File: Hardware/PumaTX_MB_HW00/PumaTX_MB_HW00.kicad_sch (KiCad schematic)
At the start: 5 parts

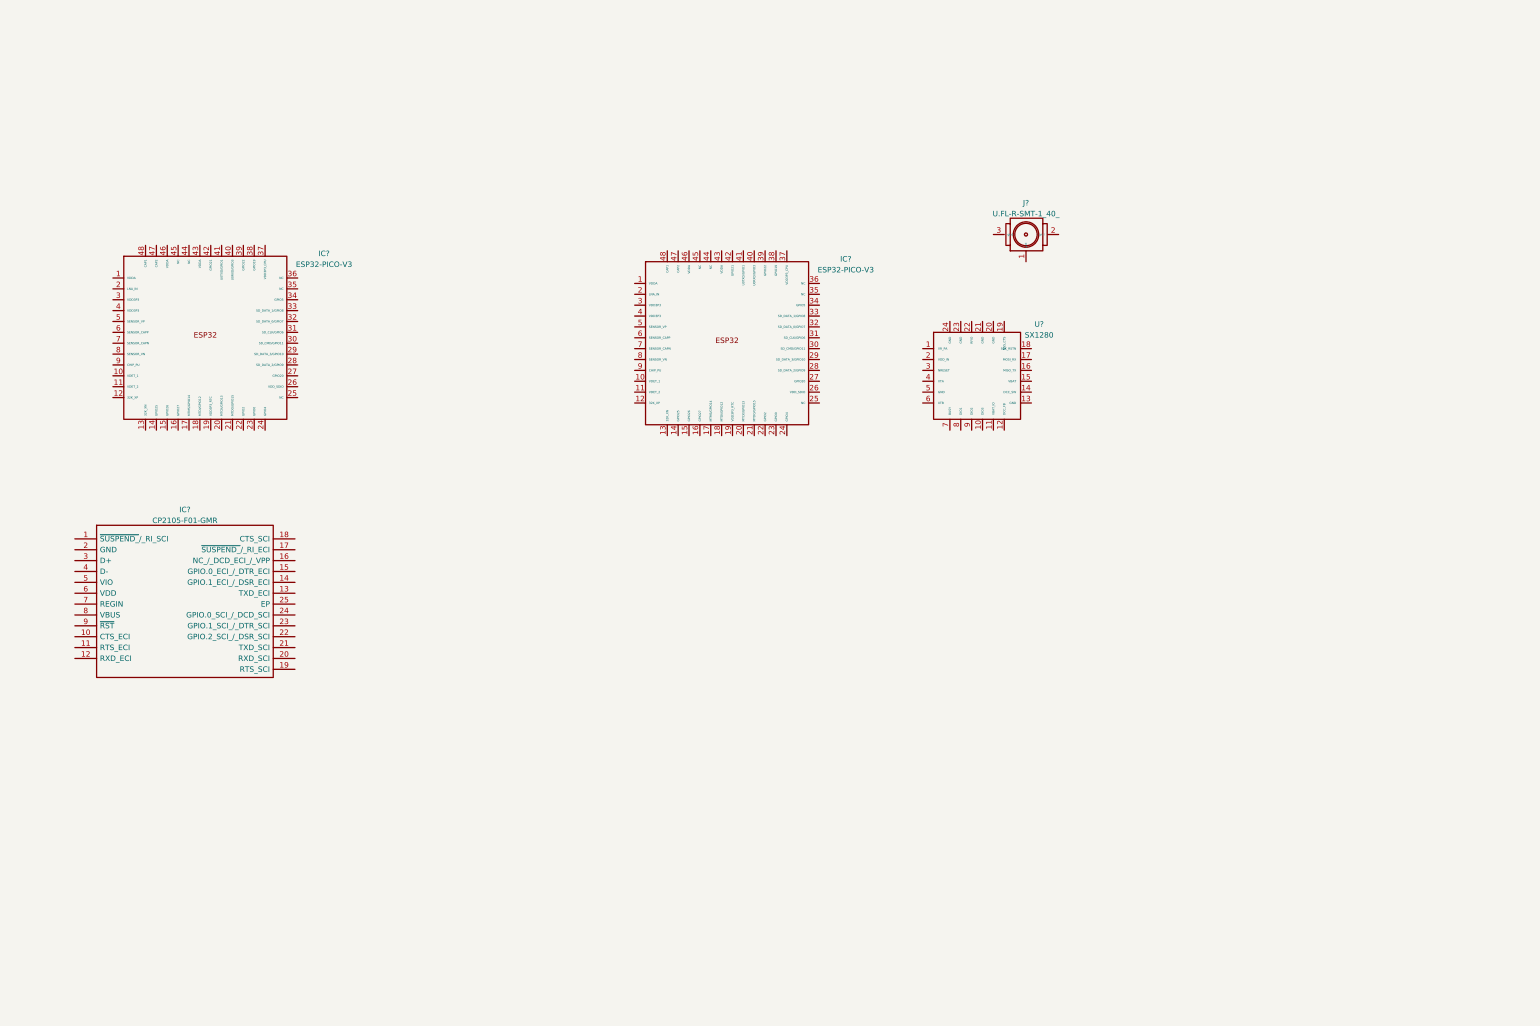
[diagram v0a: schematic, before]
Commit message: Added E28-2G4M27S
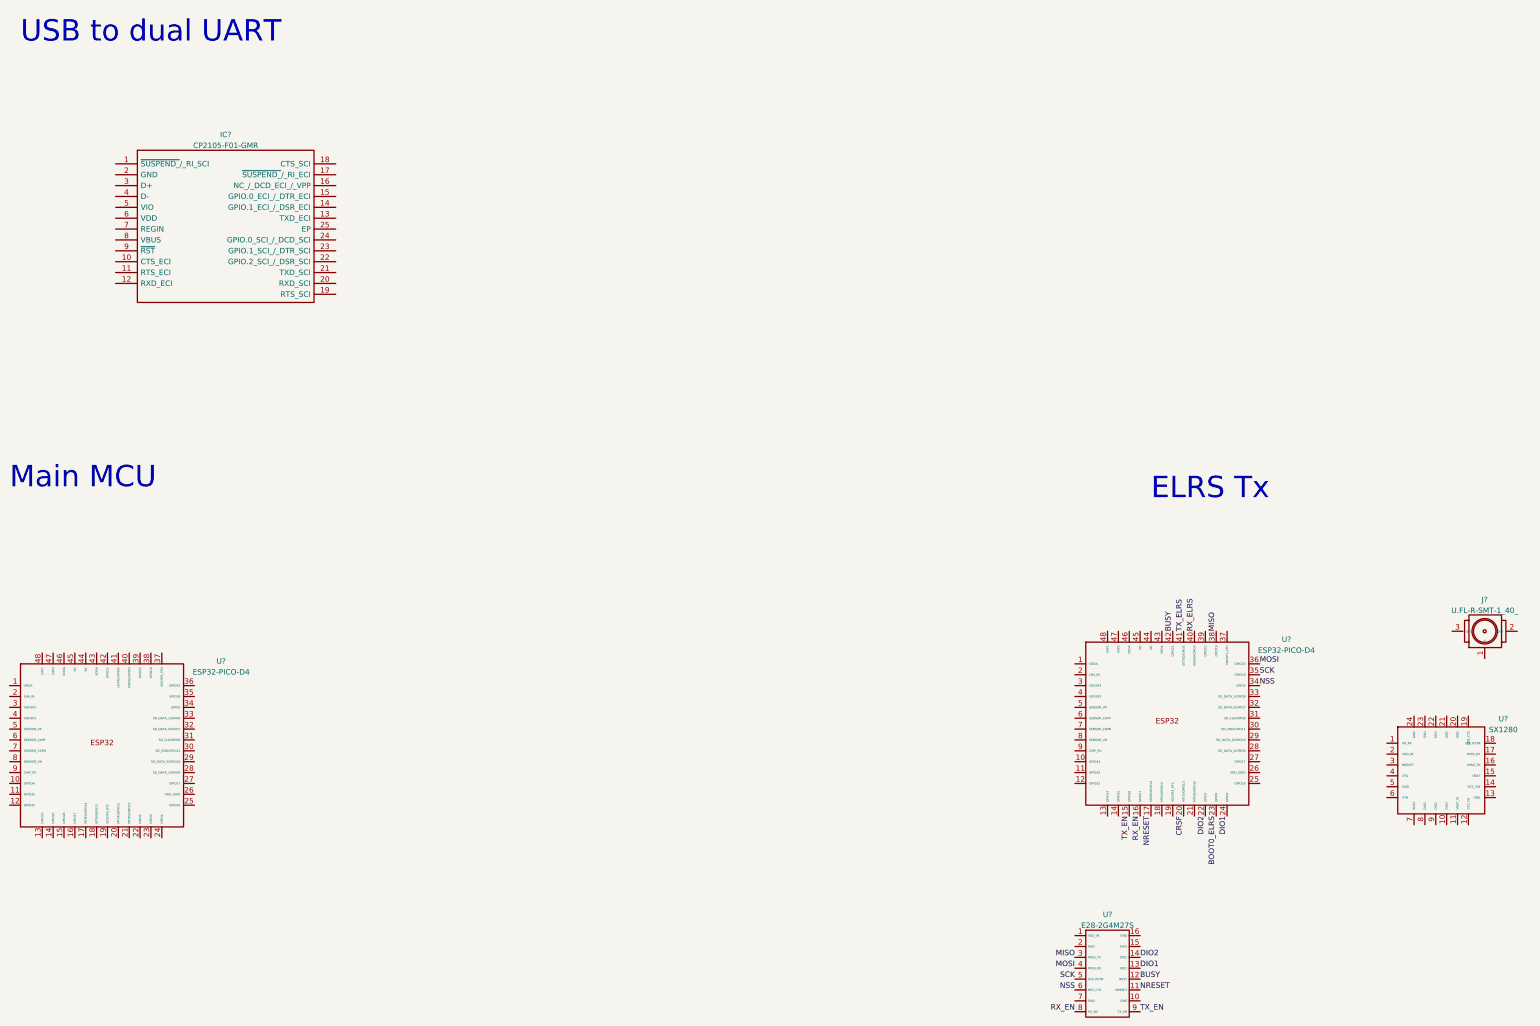
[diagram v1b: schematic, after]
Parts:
- removed IC? (x2): ESP32-PICO-V3, ESP32PICOV3, symbol Component lib:ESP32-PICO-V3
- removed U?: SX1280, symbol Component lib:SX1280
- added U? (x2): ESP32-PICO-D4, ESP32-PICO-D4_1, symbol Component_lib:ESP32-PICO-D4
- added U?: E28-2G4M27S, symbol Component_lib:E28-2G4M27S
- added U?: SX1280, Component_lib:QFN50P400X400X100-25N-D, symbol Component_lib:SX1280
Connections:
- new net BOOT0_ELRS: U?.23 (GPIO0)
- new net BUSY: U?.12 (BUSY), U?.42 (GPIO21)
- new net CRSF: U?.20 (MTCK/GPIO13)
- new net DIO1: U?.13 (DIO1), U?.24 (GPIO4)
- new net DIO2: U?.14 (DIO2), U?.22 (GPIO2)
- new net MISO: U?.3 (MISO_TX), U?.38 (GPIO19)
- new net MOSI: U?.36 (GPIO23), U?.4 (MOSI_RX)
- new net NRESET: U?.11 (NRESET), U?.17 (MTMS/GPIO14)
- new net NSS: U?.34 (GPIO5), U?.6 (NSS_CTS)
- new net RX_ELRS: U?.40 (U0RXD/GPIO3)
- new net RX_EN: U?.16 (GPIO27), U?.8 (RX_EN)
- new net SCK: U?.35 (GPIO18), U?.5 (SCK_RSTN)
- new net TX_ELRS: U?.41 (U0TXD/GPIO1)
- new net TX_EN: U?.15 (GPIO26), U?.9 (TX_EN)
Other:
- note added: "ELRS Tx"
- note added: "Main MCU"
- note added: "USB to dual UART"
- company: (none) -> PumaCorp
- title: (none) -> PumaTX_MB
- moved on the sheet: IC?, J?

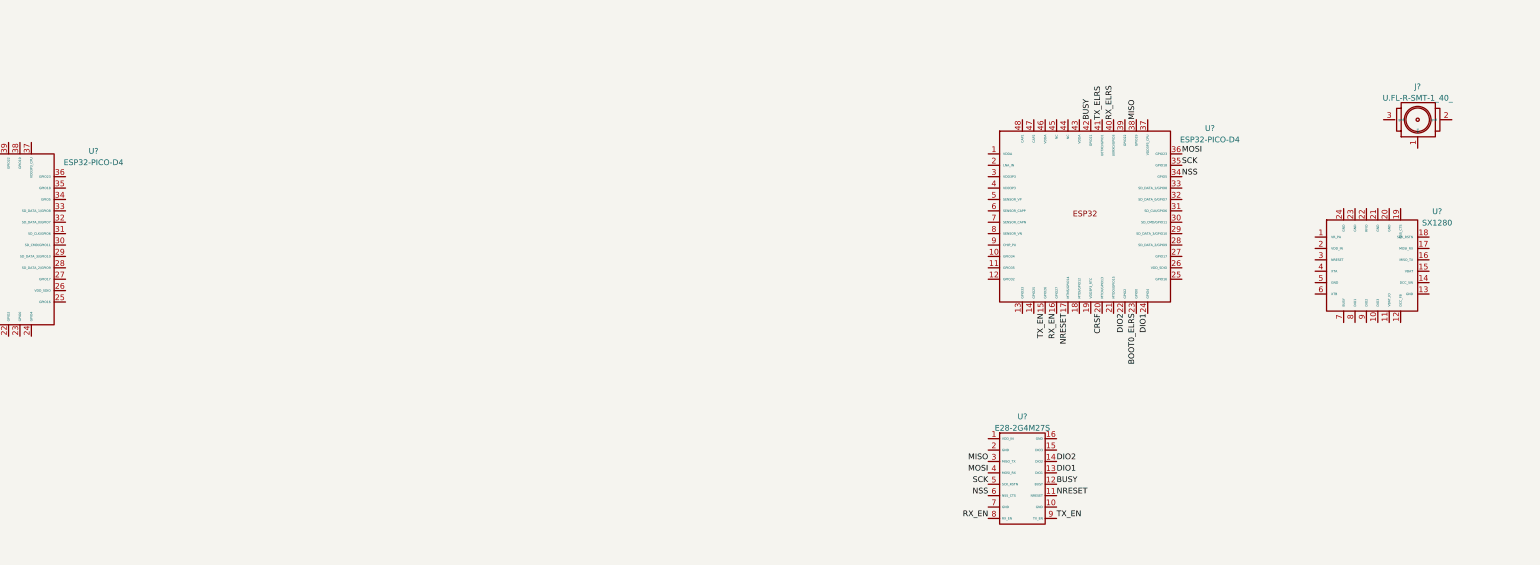
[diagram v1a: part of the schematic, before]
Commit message: Small updates around SX1280
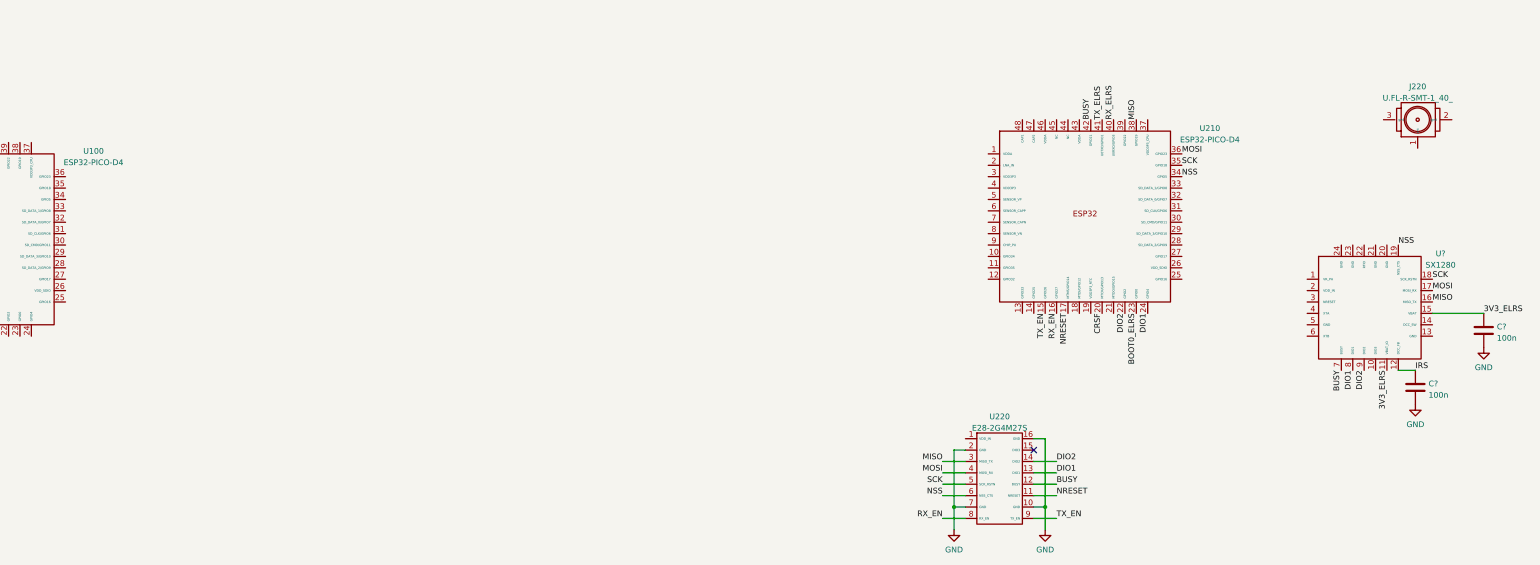
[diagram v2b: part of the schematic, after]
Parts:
- removed U?: SX1280, Component_lib:QFN50P400X400X100-25N-D, symbol Component_lib:SX1280
- added C? (x2): 100n, symbol Device:C
- added U?: SX1280, Component_lib:QFN50P400X400X100-25N-D, symbol Component_lib:SX1280
- gave numbers to parts that had none: 4
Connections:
- net BUSY: now also U?.7 (BUSY)
- net DIO1: now also U?.8 (DIO1)
- net DIO2: now also U?.9 (DIO2)
- net MISO: now also U?.16 (MISO_TX)
- net MOSI: now also U?.17 (MOSI_RX)
- net NSS: now also U?.19 (NSS_CTS)
- net SCK: now also U?.18 (SCK_RSTN)
- net GND: now reaches U220.10 (GND)
- net GND: now also U220.16 (GND), U220.2 (GND), U220.7 (GND), C?.1, C?.1
- new net 3V3_ELRS: C?.2, U?.11 (VBAT_IO), U?.15 (VBAT)
- new net IRS: C?.2, U?.12 (DCC_FB)
- no-connect marks 0 -> 1
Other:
- moved on the sheet: U220

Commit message: Updated schematic
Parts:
- removed C? (x2): 100n, symbol Device:C
- removed IC?: CP2105-F01-GMR, QFN50P400X400X80-25N-D, symbol Component lib:CP2105-F01-GMR
- added C?: 470n, symbol Component_lib:C
- added C?: 1n, symbol Component_lib:C
- added C?: 2n2, symbol Component_lib:C
- added C?: 100n, symbol Component_lib:C
- added C? (x3): 15u, symbol Component_lib:C
- added C? (x2): 10n, symbol Component_lib:C
- added J?: FH12A-26S-0.5SH_55_, FH12A26S05SH55, symbol Component_lib:FH12A-26S-0.5SH_55_
- added J?: 692122030100, 692122030100, symbol Component_lib:692122030100
- added J?: Conn_01x02_Male, symbol Connector:Conn_01x02_Male
- added J?: FH12-12S-0.5SH_55_, FH12-12S-0.5SH(55), symbol Component_lib:FH12-12S-0.5SH_55_
- added R? (x2): 2k2, symbol Component_lib:R
- added S? (x2): SKRPABE010, SKRPABE010, symbol Component_lib:SKRPABE010
- added U?: CP2105-F01-GMR, QFN50P400X400X80-25N-D, symbol Component_lib:CP2105-F01-GMR
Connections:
- net 3V3_ELRS: now also C?.1
- net CRSF: now also U100.20 (MTCK/GPIO13)
- net GND: now also J220.2 (gnd), J220.3 (gnd), U?.13 (GND), U?.20 (GND), U?.21 (GND), U?.23 (GND), U?.24 (GND), U?.5 (GND), C?.2, C?.2, C?.2, C?.2, C?.2, C?.2, C?.2, C?.2, C?.2, J?.10, J?.11, J?.3, J?.8
- net IRS: now also U?.2 (VDD_IN), C?.1, C?.1
- net NRESET: now also U?.3 (NRESET)
- net at U?.1 (VR_PA): now also C?.1
- net at U?.22 (RFIO): now also J220.1 (ant)
- net LEFT_POT: now reaches U100.11 (GPIO35)
- net RIGHT_POT: now reaches U100.12 (GPIO32)
- net BATTERY_VOLTAGE: now reaches U100.13 (GPIO33)
- net RIGHT: now reaches U100.14 (GPIO25)
- net LEFT: now reaches U100.15 (GPIO26)
- net ON_OFF: now reaches U100.16 (GPIO27)
- net UP: now reaches U100.17 (MTMS/GPIO14)
- net DOWN: now reaches U100.18 (MTDI/GPIO12)
- net RECORD: now reaches U100.21 (MTDO/GPIO15)
- net C2: now reaches U100.25 (GPIO16)
- net C1: now reaches U100.27 (GPIO17)
- net PAUSE: now reaches U100.34 (GPIO5)
- net RTH: now reaches U100.35 (GPIO18)
- net PHOTO: now reaches U100.36 (GPIO23)
- net OK: now reaches U100.38 (GPIO19)
- net LED: now reaches U100.39 (GPIO22)
- net RX_PUMATX_DEBUG: now reaches U100.40 (U0RXD/GPIO3)
- net RX_PUMATX_DEBUG: now also U?.21 (TXD_SCI)
- net TX_PUMATX_DEBUG: now reaches U100.41 (U0TXD/GPIO1)
- net TX_PUMATX_DEBUG: now also U?.20 (RXD_SCI)
- net RX_ELRS renamed RX_ELRS_DEBUG
- net RX_ELRS_DEBUG: now also U?.13 (TXD_ECI)
- net TX_ELRS renamed TX_ELRS_DEBUG
- net TX_ELRS_DEBUG: now also U?.12 (RXD_ECI)
- new net: C?.1, J?.7
- new net: C?.1, J?.1
- new net +3V3: C?.1, J?.6, R?.1, R?.1
- new net DISPLAY_BACKLIGHT: J?.12
- new net DISPLAY_SCL: C?.1, J?.5, R?.2
- new net DISPLAY_SDA: C?.1, J?.4, R?.2
- no-connect marks 1 -> 4
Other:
- note added: "Haptic motor"
- moved on the sheet: J220, U210, U220, U?

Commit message: Updated schematics
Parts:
- removed U100, U210: ESP32-PICO-D4, ESP32-PICO-D4_1, symbol Component_lib:ESP32-PICO-D4
- added C? (x2): 1u, symbol Component_lib:C
- added Q? (x2): UMH3NTN, UMH3NTN, symbol Component_lib:UMH3NTN
- added R? (x2): 10k, symbol Component_lib:R
- added U? (x2): ESP32-PICO-D4, ESP32-PICO-D4_1, symbol Component_lib:ESP32-PICO-D4
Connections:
- net +3V3: now also R?.1, R?.1
- net BATTERY_VOLTAGE: now also U?.13 (GPIO33)
- net BUSY: now also U?.42 (GPIO21)
- net C1: now also S?.1 (NO_1), S?.2 (NO_2), U?.39 (GPIO22)
- net C2: now also S?.1 (NO_1), S?.2 (NO_2), U?.38 (GPIO19)
- net CRSF: now also U?.20 (MTCK/GPIO13), U?.20 (MTCK/GPIO13)
- net DIO1: now also U?.24 (GPIO4)
- net DIO2: now also U?.22 (GPIO2)
- net DOWN: now also U?.18 (MTDI/GPIO12)
- net GND: now also C?.2, C?.2
- net LED: now also U?.42 (GPIO21)
- net LEFT: now also U?.15 (GPIO26)
- net LEFT_POT: now also U?.11 (GPIO35)
- net MISO: now also U?.38 (GPIO19)
- net MOSI: now also U?.36 (GPIO23)
- net NRESET: now also U?.17 (MTMS/GPIO14)
- net NSS: now also U?.34 (GPIO5)
- net OK: now also U?.25 (GPIO16)
- net ON_OFF: now also U?.16 (GPIO27)
- net PAUSE: now also U?.34 (GPIO5)
- net PHOTO: now also U?.36 (GPIO23)
- net RECORD: now also U?.21 (MTDO/GPIO15)
- net RIGHT: now also U?.14 (GPIO25)
- net RIGHT_POT: now also U?.12 (GPIO32)
- net RTH: now also U?.35 (GPIO18)
- net RX_ELRS_DEBUG: now also U?.40 (U0RXD/GPIO3)
- net RX_EN: now also U?.16 (GPIO27)
- net RX_PUMATX_DEBUG: now also U?.40 (U0RXD/GPIO3)
- net SCK: now also U?.35 (GPIO18)
- net TX_ELRS_DEBUG: now also U?.41 (U0TXD/GPIO1)
- net TX_EN: now also U?.15 (GPIO26)
- net TX_PUMATX_DEBUG: now also U?.41 (U0TXD/GPIO1)
- net UP: now also U?.17 (MTMS/GPIO14)
- net ELRS_RTS: now reaches U?.11 (RTS_ECI)
- net ELRS_RTS: now also Q?.1 (E1), Q?.5 (B2)
- net ELRS_DTR: now reaches U?.15 (GPIO.0_ECI_/_DTR_ECI)
- net ELRS_DTR: now also Q?.2 (B1), Q?.4 (E2)
- net PUMATX_RTS: now reaches U?.19 (RTS_SCI)
- net PUMATX_RTS: now also Q?.1 (E1), Q?.5 (B2)
- net PUMATX_DTR: now reaches U?.23 (GPIO.1_SCI_/_DTR_SCI)
- net PUMATX_DTR: now also Q?.2 (B1), Q?.4 (E2)
- new net ELRS_CHIP_PU: C?.1, Q?.6 (C1), R?.2, U?.9 (CHIP_PU)
- new net ELRS_GPIO0: Q?.3 (C2), U?.23 (GPIO0)
- new net PUMATX_CHIP_PU: C?.1, Q?.6 (C1), R?.2, U?.9 (CHIP_PU)
- new net PUMATX_GPIO0: Q?.3 (C2), U?.23 (GPIO0)
- no-connect marks 4 -> 17

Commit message: Updated schematic
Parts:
- added J? (x2): Conn_01x02_Male, symbol Connector:Conn_01x02_Male
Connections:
- net DISPLAY_BACKLIGHT: now also U?.24 (GPIO4)
- net DISPLAY_SCL: now also U?.14 (GPIO25)
- net DISPLAY_SDA: now also U?.15 (GPIO26)
- net DOWN: now also U?.8 (SENSOR_VN/GPIO39); no longer U?.18 (MTDI/GPIO12)
- net LED: now also U?.22 (GPIO2); no longer U?.42 (GPIO21)
- net LEFT: now also U?.6 (SENSOR_CAPP/GPIO37); no longer U?.15 (GPIO26)
- net ON_OFF: now also U?.10 (GPIO34); no longer U?.16 (GPIO27)
- net RIGHT: now also U?.5 (SENSOR_VP/GPIO36); no longer U?.14 (GPIO25)
- net UP: now also U?.7 (SENSOR_CAPN/GPIO38); no longer U?.17 (MTMS/GPIO14)
- new net BUZZER_PWM: U?.16 (GPIO27)
- new net FAN_PWM: U?.17 (MTMS/GPIO14)
- new net HAPTIC_PWM: U?.18 (MTDI/GPIO12)
- no-connect marks 17 -> 28
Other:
- note added: "Buzzer"
- note added: "Fan"
- moved on the sheet: U?

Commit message: Started a rough layout
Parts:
- added J102, J103: 500334-0160, Component_lib:5003340160, symbol Component lib:500334-0160
- C101, C102, C103, C300, C301, C302, C401, C410, C411: renamed from C?; footprint (none) -> Capacitor_SMD:C_0402_1005Metric
- C412, C413: renamed from C?; footprint (none) -> Capacitor_SMD:C_0603_1608Metric
- J100: renamed from J?; footprint FH12A26S05SH55 -> Component_lib:FH12A26S05SH55
- J104: renamed from J?; footprint 692122030100 -> Component_lib:692122030100
- J105, J106, J107: renamed from J?; footprint (none) -> Connector_PinHeader_1.27mm:PinHeader_1x02_P1.27mm_Horizontal
- J410: renamed from J220; footprint UFLRSMT140 -> Component_lib:u.fl
- Q200, Q201: renamed from Q?; footprint UMH3NTN -> Component_lib:UMH3NTN
- R300, R301, R302, R401: renamed from R?; footprint (none) -> Capacitor_SMD:C_0402_1005Metric
- S100, S101: renamed from S?; footprint SKRPABE010 -> Component_lib:SKRPABE010
- U200: renamed from U?; footprint QFN50P400X400X80-25N-D -> Component_lib:QFN50P400X400X80-25N-D
- U300, U400: renamed from U?; footprint ESP32-PICO-D4_1 -> Component_lib:ESP32-PICO-D4_1
- U402: renamed from U220; footprint (none) -> Component_lib:E28-2G4M27S
- gave numbers to parts that had none: 2
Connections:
- net +3V3: now also J102.11, J102.5, J102.8, J103.12, J103.6, J103.9
- net GND: now also J102.10, J102.13, J102.14, J102.2, J102.3, J102.7, J103.10, J103.14, J103.15, J103.3, J103.4, J103.7
- net LEFT_POT: now also J102.1
- net RIGHT_POT: now also J103.16
- net SPORT: now reaches U300.42 (GPIO21)
- net SPORT: now also J103.5
- net DISPLAY_SCL renamed PUMATX_SCL
- net PUMATX_SCL: now also J102.15, J103.2
- net DISPLAY_SDA renamed PUMATX_SDA
- net PUMATX_SDA: now also J102.16, J103.1
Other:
- note added: "100- RC interface"
- note added: "200- USB to dual UART"
- note added: "300- Main MCU"
- note added: "400- ELRS Tx"
- note removed: "ELRS Tx"
- note removed: "Main MCU"
- note removed: "USB to dual UART"
- moved on the sheet: C101, C102, C103, C300, C301, C302, C401, C410, C411, C412, C413, J100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

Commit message: Started working on the power part
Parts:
- removed J104: 692122030100, Component_lib:692122030100, symbol Component_lib:692122030100
- added C501: 1u, symbol Component lib:C
- added C502, C503: 4u7, symbol Component lib:C
- added C510, C511, C520, C521, C530, C531: 2u2, symbol Component lib:C
- added J105: 53398-0667, 533980667, symbol Component lib:53398-0667
- added J?: 692122030100, 692122030100, symbol Component lib:692122030100
- added U500: BQ24075RGTR, QFN50P300X300X100-17N-D, symbol Component lib:BQ24075RGTR
- added U510, U520, U530: MIC5528-3.3YMT-T5, SON40P120X120X60-7N-D, symbol Component lib:MIC5528-3.3YMT-T5
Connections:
- net CRSF: now also J?.6 (SSRX+)
- net GND: now also C501.2, C502.2, C503.2, C510.2, C511.2, C520.2, C521.2, C530.2, C531.2, J105.3, J105.4, J?.10 (SHIELD), J?.4 (GND), J?.MH1, J?.MH2, U500.17 (GND), U500.8 (VSS), U510.3 (GND), U510.7 (EP), U520.3 (GND), U520.7 (EP), U530.3 (GND), U530.7 (EP)
- net PUMATX_SCL: now also J?.9 (SSTX+)
- net PUMATX_SDA: now also J?.8 (SSTX-)
- net SX1280_3V3: now reaches U402.1 (VDD_IN)
- net SX1280_3V3: now also C531.1, U530.1 (VOUT_1), U530.2 (VOUT_2)
- new net: C520.1, U520.6 (VIN)
- new net: C510.1, U510.6 (VIN)
- new net: C530.1, U530.6 (VIN)
- new net: J105.5, J105.6
- new net: U500.10 (OUT_1), U500.11 (OUT_2)
- new net: U500.2 (BAT_1), U500.3 (BAT_2)
- new net BATTERY_TEMP: J105.2, U500.1 (TS)
- new net BATTERY_WHITE: J105.1
- new net ELRS_ESP32_3V3: C521.1, U520.1 (VOUT_1), U520.2 (VOUT_2)
- new net PUMATX_ESP32_3V3: C511.1, J?.3 (D+), U510.1 (VOUT_1), U510.2 (VOUT_2)
- new net VBUS: C501.1, J?.1 (VBUS), U500.13 (IN)
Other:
- note added: "500- Power"
- moved on the sheet: C401, R401, U400
